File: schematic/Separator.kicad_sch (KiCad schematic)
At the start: 2 parts

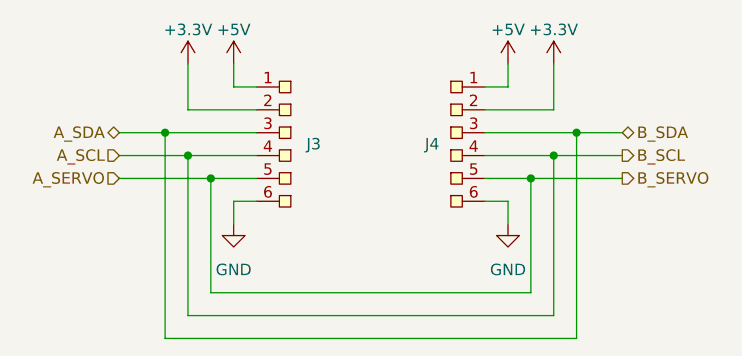
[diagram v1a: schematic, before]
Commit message: Assign footprints
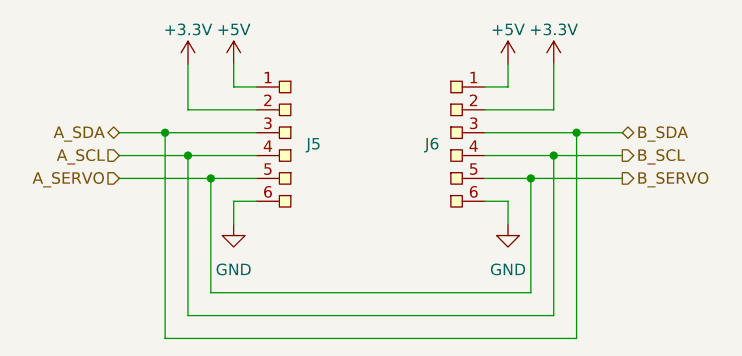
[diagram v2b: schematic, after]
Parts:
- renumbered J3 to J5, J4 to J6
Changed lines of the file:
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@@
   (symbol (lib_id "Custom:SolderPad-6pin") (at 152.4 95.25 0) (unit 1)
     (in_bom no) (on_board yes) (dnp no)
-    (property "Reference" "J4" (at 147.32 95.25 0)
+    (property "Reference" "J6" (at 147.32 95.25 0)
       (effects (font (size 1.27 1.27)) (justify right))
     )
@@
       (project "ISSptr"
         (path "/c978750c-b285-44b2-8d41-37a456977bcd/fc6af4d0-251f-4908-9d3e-0df25c48aee5"
-          (reference "J4") (unit 1)
+          (reference "J6") (unit 1)
         )
       )
@@
   (symbol (lib_id "Custom:SolderPad-6pin") (at 127 95.25 0) (mirror y) (unit 1)
     (in_bom no) (on_board yes) (dnp no)
-    (property "Reference" "J3" (at 133.35 95.25 0)
+    (property "Reference" "J5" (at 133.35 95.25 0)
       (effects (font (size 1.27 1.27)))
     )
@@
       (project "ISSptr"
         (path "/c978750c-b285-44b2-8d41-37a456977bcd/fc6af4d0-251f-4908-9d3e-0df25c48aee5"
-          (reference "J3") (unit 1)
+          (reference "J5") (unit 1)
         )
       )
